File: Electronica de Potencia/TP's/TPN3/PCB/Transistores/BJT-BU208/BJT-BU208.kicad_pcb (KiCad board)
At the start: 2 copper layers, 100.7 x 69.3 mm, 25 parts, among them J1 Vin, J2 PWM_IN, Q1 BC548, Q2 BC558, Q3 BU208, U1 L7812, U2 L7905

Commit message: 22
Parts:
- added G1: logo, lib_fp:logo_utn_fsilk_small, F.Cu at (152.4, 55.9)
- moved TP1 17.9 mm to (160.6, 55.9)
- moved TP2 14.2 mm to (160.0, 106.7)
- moved J1 11.3 mm to (73.8, 52.0), turned to 0 degrees
- moved TP3 3.83 mm to (160.7, 81.3)
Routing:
- net +15V: track 119.5 -> 137.6 mm
- net Net-(D1-Pad1): track 101.7 -> 117.9 mm
- net Net-(Q1-Pad2): track 68.0 -> 68.8 mm
- net Net-(JP2-Pad2): track 80.0 -> 79.3 mm

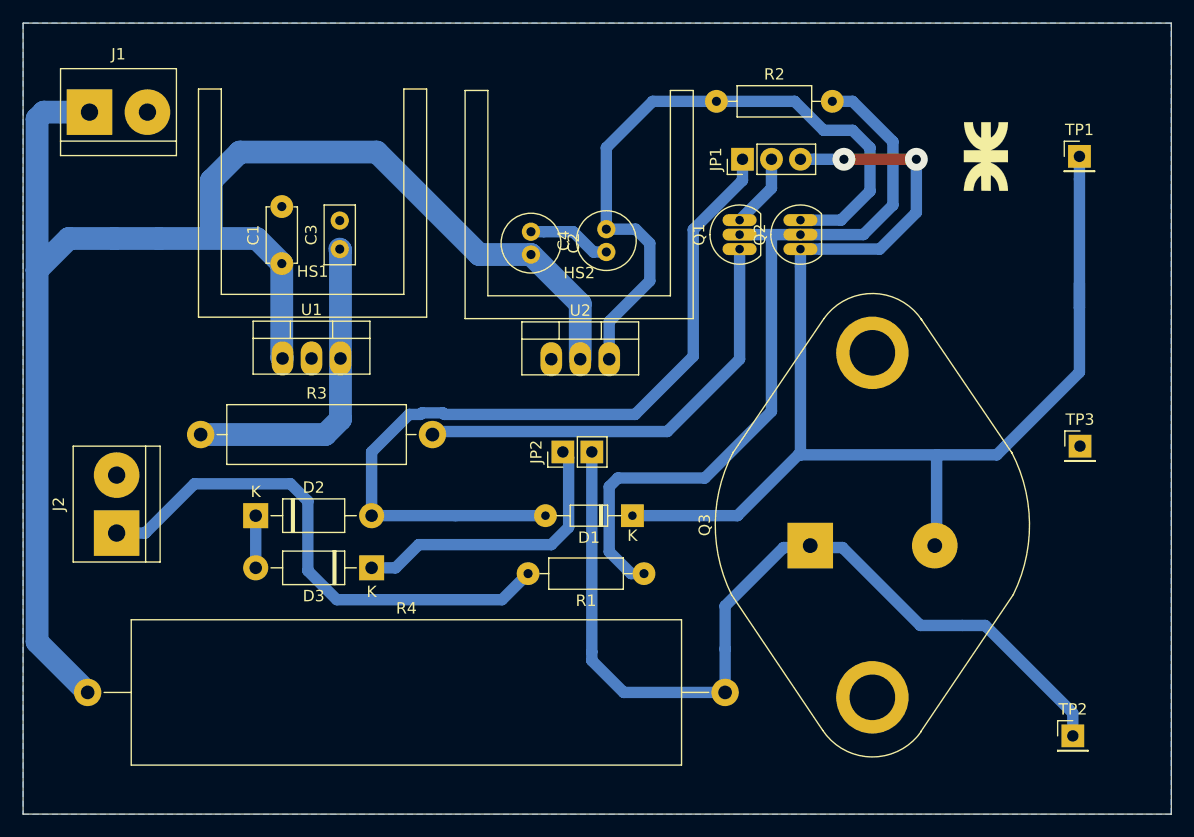
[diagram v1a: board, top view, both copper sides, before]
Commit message: Placa TP3 transistor completa
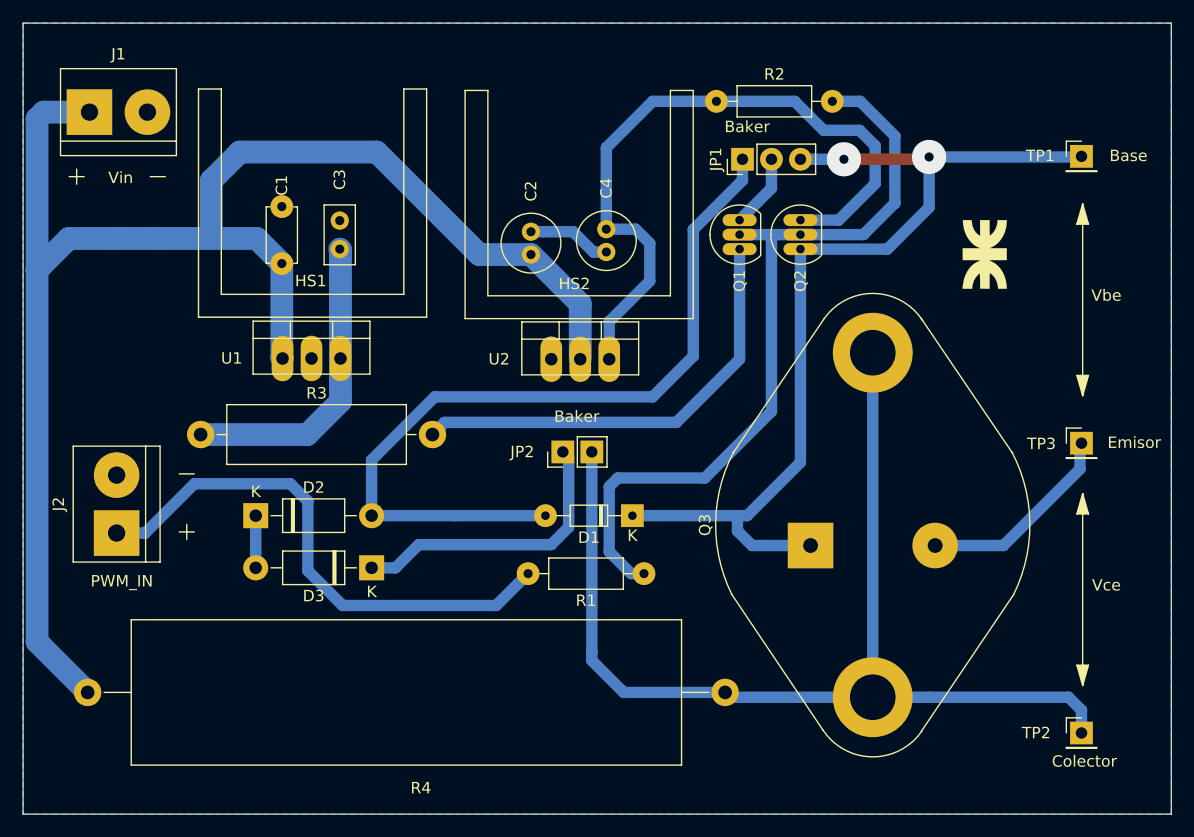
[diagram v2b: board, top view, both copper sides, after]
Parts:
- moved G1 8.59 mm to (152.3, 64.5)
- moved TP2 0.80 mm to (160.8, 106.4)
- moved TP3 0.29 mm to (160.8, 81.0)
- moved TP1 0.18 mm to (160.8, 55.9)
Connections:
- C2 pad 1: Net-(C2-Pad1) -> GND
- C4 pad 1: Net-(C2-Pad1) -> GND
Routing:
- net Net-(D1-Pad1): track 117.9 -> 86.0 mm
- net GND: track 0.00 -> 24.8 mm
- net Net-(JP2-Pad2): track 79.3 -> 95.2 mm
- net Net-(C2-Pad1): track 7.34 -> 0.00 mm
- net +12V: track 27.8 -> 26.8 mm
- net -5V: track 60.5 -> 61.2 mm
- net Net-(Q1-Pad2): track 68.8 -> 69.4 mm
- net Net-(D1-Pad2): track 71.7 -> 71.1 mm
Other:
- board text added: "-"
- board text added: "Baker"
- board text added: "Base"
- board text added: "Colector"
- board text added: "Emisor"
- board text added: "PWM_IN"
- board text added: "Vbe"
- board text added: "Vce"
- board text added: "Vin"
